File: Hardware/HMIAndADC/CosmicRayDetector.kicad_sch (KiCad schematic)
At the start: 0 parts

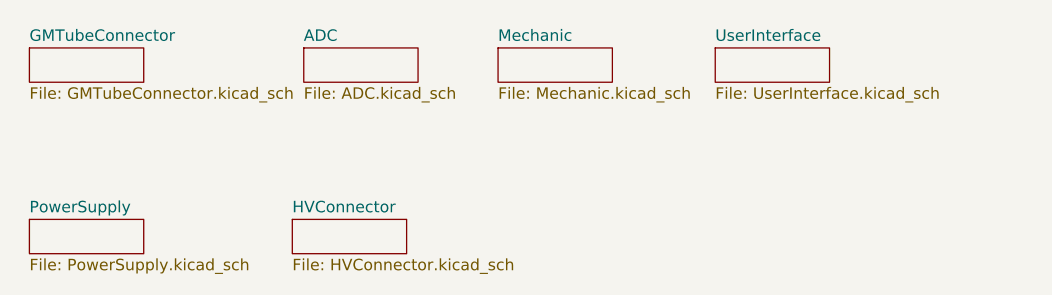
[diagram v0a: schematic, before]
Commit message: split pcb dsign to separate pcbs
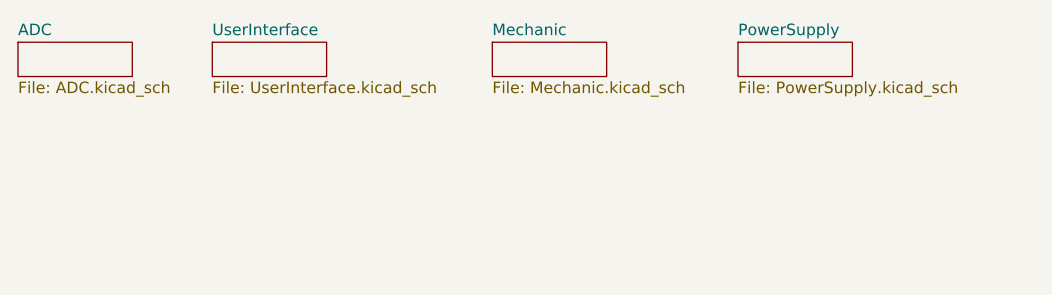
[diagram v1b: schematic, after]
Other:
- removed sheet GMTubeConnector
- removed sheet HVConnector
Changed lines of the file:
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@@
 (kicad_sch (version 20210621) (generator eeschema)
   (paper "A4")
-  (sheet (at 105.41 45.72) (size 12.7 3.81) (fields_autoplaced)
-    (stroke (width 0) (type solid) (color 0 0 0 0))
-    (fill (color 0 0 0 0.0000))
-    (property "Sheet name" "ADC" (id 0) (at 105.41 45.0845 0)
-      (effects (font (size 1.27 1.27)) (justify left bottom))
-    )
-    (property "Sheet file" "ADC.kicad_sch" (id 1) (at 105.41 50.0385 0)
-      (effects (font (size 1.27 1.27)) (justify left top))
-    )
-  )
-  (sheet (at 74.93 45.72) (size 12.7 3.81) (fields_autoplaced)
-    (stroke (width 0) (type solid) (color 0 0 0 0))
-    (fill (color 0 0 0 0.0000))
-    (property "Sheet name" "GMTubeConnector" (id 0) (at 74.93 45.0845 0)
-      (effects (font (size 1.27 1.27)) (justify left bottom))
-    )
-    (property "Sheet file" "GMTubeConnector.kicad_sch" (id 1) (at 74.93 50.0385 0)
-      (effects (font (size 1.27 1.27)) (justify left top))
-    )
-  )
-  (sheet (at 104.14 64.77) (size 12.7 3.81) (fields_autoplaced)
-    (stroke (width 0) (type solid) (color 0 0 0 0))
-    (fill (color 0 0 0 0.0000))
-    (property "Sheet name" "HVConnector" (id 0) (at 104.14 64.1345 0)
-      (effects (font (size 1.27 1.27)) (justify left bottom))
-    )
-    (property "Sheet file" "HVConnector.kicad_sch" (id 1) (at 104.14 69.0885 0)
-      (effects (font (size 1.27 1.27)) (justify left top))
-    )
-  )
-  (sheet (at 127 45.72) (size 12.7 3.81) (fields_autoplaced)
-    (stroke (width 0) (type solid) (color 0 0 0 0))
-    (fill (color 0 0 0 0.0000))
-    (property "Sheet name" "Mechanic" (id 0) (at 127 45.0845 0)
-      (effects (font (size 1.27 1.27)) (justify left bottom))
-    )
-    (property "Sheet file" "Mechanic.kicad_sch" (id 1) (at 127 50.0385 0)
-      (effects (font (size 1.27 1.27)) (justify left top))
-    )
-  )
-  (sheet (at 74.93 64.77) (size 12.7 3.81) (fields_autoplaced)
-    (stroke (width 0) (type solid) (color 0 0 0 0))
-    (fill (color 0 0 0 0.0000))
-    (property "Sheet name" "PowerSupply" (id 0) (at 74.93 64.1345 0)
-      (effects (font (size 1.27 1.27)) (justify left bottom))
-    )
-    (property "Sheet file" "PowerSupply.kicad_sch" (id 1) (at 74.93 69.0885 0)
-      (effects (font (size 1.27 1.27)) (justify left top))
-    )
-  )
-  (sheet (at 151.13 45.72) (size 12.7 3.81) (fields_autoplaced)
-    (stroke (width 0) (type solid) (color 0 0 0 0))
-    (fill (color 0 0 0 0.0000))
-    (property "Sheet name" "UserInterface" (id 0) (at 151.13 45.0845 0)
-      (effects (font (size 1.27 1.27)) (justify left bottom))
-    )
-    (property "Sheet file" "UserInterface.kicad_sch" (id 1) (at 151.13 50.0385 0)
+  (sheet (at 73.66 45.085) (size 12.7 3.81) (fields_autoplaced)
+    (stroke (width 0) (type solid) (color 0 0 0 0))
+    (fill (color 0 0 0 0.0000))
+    (property "Sheet name" "ADC" (id 0) (at 73.66 44.4495 0)
+      (effects (font (size 1.27 1.27)) (justify left bottom))
+    )
+    (property "Sheet file" "ADC.kicad_sch" (id 1) (at 73.66 49.4035 0)
+      (effects (font (size 1.27 1.27)) (justify left top))
+    )
+  )
+  (sheet (at 126.365 45.085) (size 12.7 3.81) (fields_autoplaced)
+    (stroke (width 0) (type solid) (color 0 0 0 0))
+    (fill (color 0 0 0 0.0000))
+    (property "Sheet name" "Mechanic" (id 0) (at 126.365 44.4495 0)
+      (effects (font (size 1.27 1.27)) (justify left bottom))
+    )
+    (property "Sheet file" "Mechanic.kicad_sch" (id 1) (at 126.365 49.4035 0)
+      (effects (font (size 1.27 1.27)) (justify left top))
+    )
+  )
+  (sheet (at 153.67 45.085) (size 12.7 3.81) (fields_autoplaced)
+    (stroke (width 0) (type solid) (color 0 0 0 0))
+    (fill (color 0 0 0 0.0000))
+    (property "Sheet name" "PowerSupply" (id 0) (at 153.67 44.4495 0)
+      (effects (font (size 1.27 1.27)) (justify left bottom))
+    )
+    (property "Sheet file" "PowerSupply.kicad_sch" (id 1) (at 153.67 49.4035 0)
+      (effects (font (size 1.27 1.27)) (justify left top))
+    )
+  )
+  (sheet (at 95.25 45.085) (size 12.7 3.81) (fields_autoplaced)
+    (stroke (width 0) (type solid) (color 0 0 0 0))
+    (fill (color 0 0 0 0.0000))
+    (property "Sheet name" "UserInterface" (id 0) (at 95.25 44.4495 0)
+      (effects (font (size 1.27 1.27)) (justify left bottom))
+    )
+    (property "Sheet file" "UserInterface.kicad_sch" (id 1) (at 95.25 49.4035 0)
       (effects (font (size 1.27 1.27)) (justify left top))
     )
@@
     (path "/" (page "1"))
     (path "/00000000-0000-0000-0000-00005cef836a" (page "2"))
-    (path "/00000000-0000-0000-0000-00005fa35ce1" (page "3"))
-    (path "/00000000-0000-0000-0000-00005fa2327e" (page "4"))
     (path "/00000000-0000-0000-0000-00005f9e7696" (page "5"))
     (path "/00000000-0000-0000-0000-00005fa5724c" (page "6"))
@@
       (reference "J2") (unit 1) (value "Conn_02x06_Odd_Even") (footprint "Connector_PinHeader_2.54mm:PinHeader_2x06_P2.54mm_Horizontal")
     )
-    (path "/00000000-0000-0000-0000-00005fa2327e/00000000-0000-0000-0000-00005fa3afb4"
-      (reference "J3") (unit 1) (value "Conn_01x01_Female") (footprint "TestPoint:TestPoint_Loop_D2.60mm_Drill1.4mm_Beaded")
-    )
-    (path "/00000000-0000-0000-0000-00005fa35ce1/00000000-0000-0000-0000-00005fa36ace"
-      (reference "J4") (unit 1) (value "Conn_01x01_Female") (footprint "CosmicRayDetector:GeigerTube")
-    )
-    (path "/00000000-0000-0000-0000-00005fa35ce1/00000000-0000-0000-0000-00005fa36b5f"
-      (reference "J5") (unit 1) (value "Conn_01x01_Female") (footprint "CosmicRayDetector:GeigerTube")
-    )
-    (path "/00000000-0000-0000-0000-00005fa35ce1/00000000-0000-0000-0000-00005fa36e08"
-      (reference "J6") (unit 1) (value "Conn_01x01_Female") (footprint "CosmicRayDetector:GeigerTube")
-    )
-    (path "/00000000-0000-0000-0000-00005fa35ce1/00000000-0000-0000-0000-00005fa37033"
-      (reference "J7") (unit 1) (value "Conn_01x01_Female") (footprint "CosmicRayDetector:GeigerTube")
-    )
     (path "/00000000-0000-0000-0000-00005fa5724c/8f972bce-1676-41ca-b06f-4b159cb8e6fe"
       (reference "J8") (unit 1) (value "USB_B_Micro") (footprint "Connector_USB:USB_Micro-B_Molex-105017-0001")
@@
       (reference "R21") (unit 1) (value "10k") (footprint "Resistor_SMD:R_0805_2012Metric_Pad1.15x1.40mm_HandSolder")
     )
-    (path "/00000000-0000-0000-0000-00005fa2327e/00000000-0000-0000-0000-00005fa2fa96"
-      (reference "R22") (unit 1) (value "5M1") (footprint "Resistor_THT:R_Axial_DIN0411_L9.9mm_D3.6mm_P12.70mm_Horizontal")
-    )
-    (path "/00000000-0000-0000-0000-00005fa2327e/00000000-0000-0000-0000-00005fa384db"
-      (reference "R23") (unit 1) (value "5M1") (footprint "Resistor_THT:R_Axial_DIN0411_L9.9mm_D3.6mm_P12.70mm_Horizontal")
-    )
-    (path "/00000000-0000-0000-0000-00005fa2327e/00000000-0000-0000-0000-00005fa3866d"
-      (reference "R24") (unit 1) (value "5M1") (footprint "Resistor_THT:R_Axial_DIN0411_L9.9mm_D3.6mm_P12.70mm_Horizontal")
-    )
-    (path "/00000000-0000-0000-0000-00005fa2327e/00000000-0000-0000-0000-00005fa387bb"
-      (reference "R25") (unit 1) (value "5M1") (footprint "Resistor_THT:R_Axial_DIN0411_L9.9mm_D3.6mm_P12.70mm_Horizontal")
-    )
     (path "/00000000-0000-0000-0000-00005fa231f7/00000000-0000-0000-0000-00005fa94e65"
